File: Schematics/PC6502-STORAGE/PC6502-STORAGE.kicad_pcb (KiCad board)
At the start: 4 copper layers, 100 x 100 mm, 82 parts, among them J1 BUS, J2 Conn_02x26_Top_Bottom, J3 CLK_SLOW, J5 USB_C_Receptacle_USB2.0_16P, J6 ST4500 PROG, J7 Conn_02x05_Odd_Even, J8 TF-15X15, J99 Conn_02x05_Odd_Even, Q1 STL9P3LLH6, U1 ATF1502AS, U2 STUSB4500QTR, U3 ATF1502AS, U4 TXB0108PW, U5 AMS1117-3.3

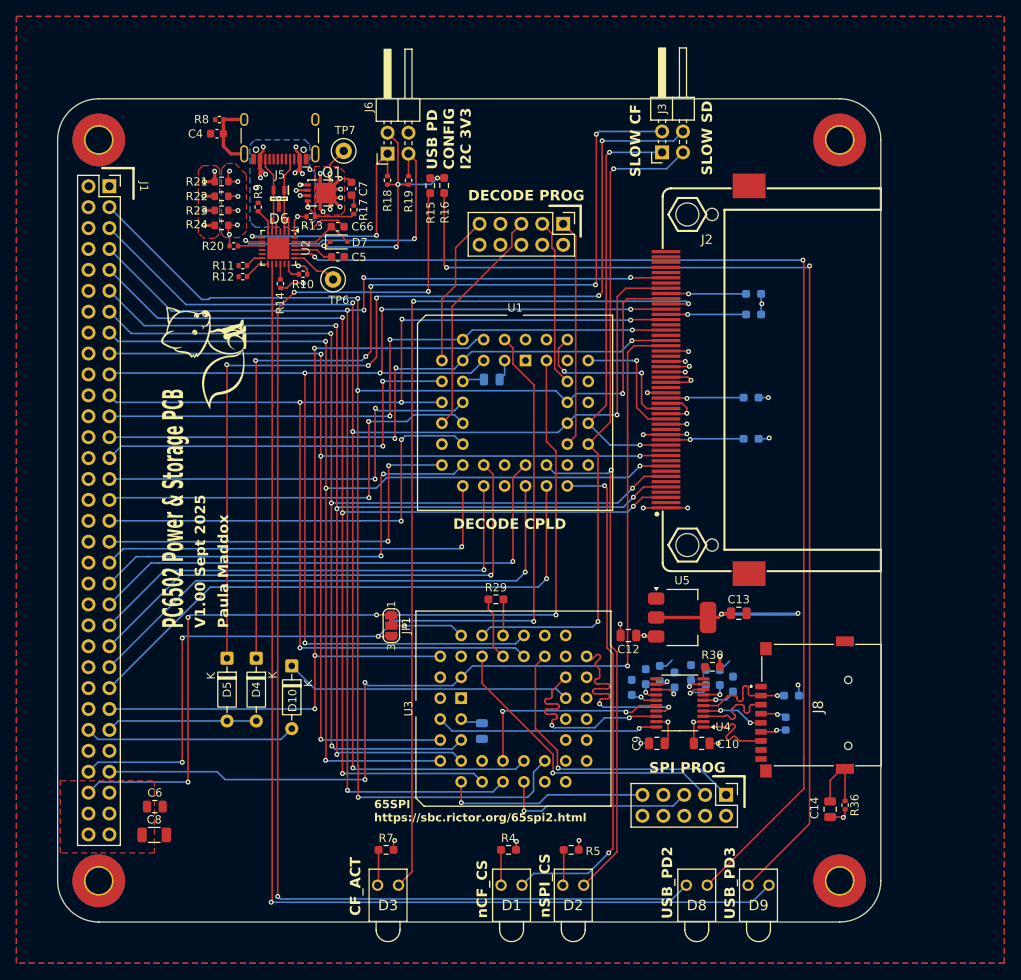
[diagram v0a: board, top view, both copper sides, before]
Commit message: Tidy up and simplify
Created schematic for FM & Speech sound board
Made Storage board just for Compact Flash (CF) storage
Routed Storage PCB
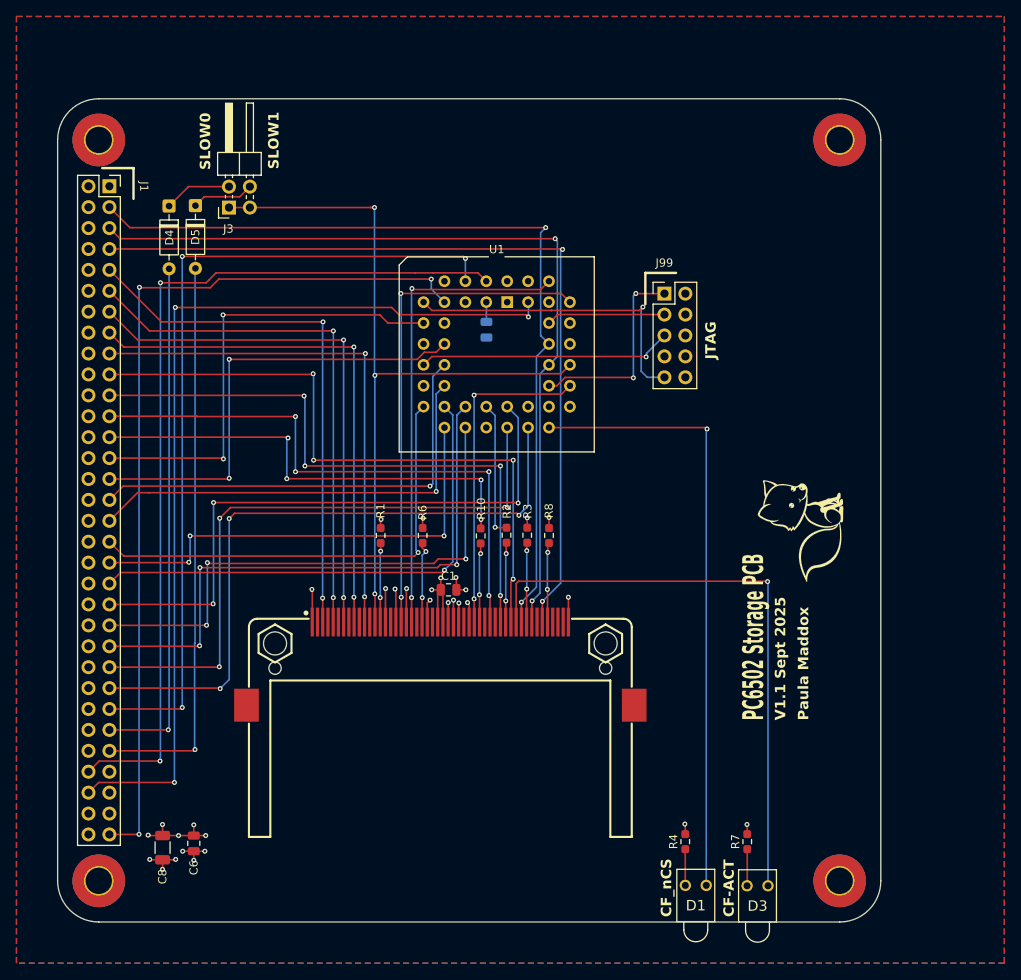
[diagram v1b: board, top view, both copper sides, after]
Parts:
- removed C10, C9: 100nF, Capacitor_SMD:C_0805_2012Metric
- removed C11, C7: 0.1uF, Capacitor_SMD:C_0603_1608Metric
- removed C12, C13: 10uF, Capacitor_SMD:C_0805_2012Metric
- removed C14: 100nF 100V, Capacitor_SMD:C_0805_2012Metric
- removed C4: 100nF 100V, Capacitor_SMD:C_0603_1608Metric
- removed C5, C66: 1uF, Capacitor_SMD:C_0603_1608Metric
- removed D10: 1N4148, Diode_THT:D_DO-35_SOD27_P7.62mm_Horizontal
- removed D2, D8, D9: LED, LTL-4221NHBP:LTL4221NHBP
- removed D6: ESDA25W, ESDA25W:SOT65P210X110-3N
- removed D7: BAT60A, Diode_SMD:D_SOD-323
- removed J5: USB_C_Receptacle_USB2.0_16P, Connector_USB:USB_C_Receptacle_HCTL_HC-TYPE-C-16P-01A
- removed J6: ST4500 PROG, Connector_PinHeader_2.54mm:PinHeader_2x02_P2.54mm_Horizontal
- removed J7: Conn_02x05_Odd_Even, Connector_PinHeader_2.54mm:PinHeader_2x05_P2.54mm_Vertical
- removed J8: TF-15X15, TF-15X15:TF15X15
- removed JP1: Jumper_3_Bridged12, Jumper:SolderJumper-3_P1.3mm_Bridged12_RoundedPad1.0x1.5mm_NumberLabels
- removed Q1: STL9P3LLH6, STL9P3LLH6:STL20N6F7
- removed R11, R12, R18, R19: 5K1, Resistor_SMD:R_0402_1005Metric
- removed R13, R9: 100K, Resistor_SMD:R_0402_1005Metric
- removed R14: 22K, Resistor_SMD:R_0402_1005Metric
- removed R15, R16, R5: 470R, Resistor_SMD:R_0603_1608Metric_Pad0.98x0.95mm_HandSolder
- removed R17: 100R, Resistor_SMD:R_0402_1005Metric
- removed R20: 1K, Resistor_SMD:R_0402_1005Metric
- removed R21, R22, R23, R24: 0R, Resistor_SMD:R_0603_1608Metric
- removed R25, R26, R27, R28, R29, R30, R31, R32, R33, R34, R35: 10K, Resistor_SMD:R_0603_1608Metric_Pad0.98x0.95mm_HandSolder
- removed R36: 330R, Resistor_SMD:R_0402_1005Metric
- removed TP6, TP7: TestPoint, TestPoint:TestPoint_Loop_D1.80mm_Drill1.0mm_Beaded
- removed U2: STUSB4500QTR, Package_DFN_QFN:QFN-24-1EP_4x4mm_P0.5mm_EP2.7x2.7mm
- removed U3: ATF1502AS, Package_LCC:PLCC-44_THT-Socket
- removed U4: TXB0108PW, Package_SO:TSSOP-20_4.4x6.5mm_P0.65mm
- removed U5: AMS1117-3.3, Package_TO_SOT_SMD:SOT-223-3_TabPin2
- C1, R1, R2, R3, R6: moved to F.Cu
- R10: value 1K -> 0R; footprint Resistor_SMD:R_0402_1005Metric -> Resistor_SMD:R_0603_1608Metric_Pad0.98x0.95mm_HandSolder
- R8: value 330R -> 1K; footprint Resistor_SMD:R_0402_1005Metric -> Resistor_SMD:R_0603_1608Metric_Pad0.98x0.95mm_HandSolder
- moved FOX1 75.5 mm to (187.3, 96.8)
- moved R8 64.5 mm to (156.8, 98.0), turned to 90 degrees
- moved D4 55.9 mm to (110.6, 58.0)
- moved D5 55.1 mm to (113.8, 58.0)
- moved J3 53.0 mm to (117.9, 58.2)
- moved C2 48.8 mm to (149.2, 73.0)
- moved J2 47.4 mm to (143.6, 113.6), turned to 0 degrees
- moved R1 46.5 mm to (136.3, 98.0), turned to 90 degrees
- moved D3 44.9 mm to (180.8, 140.6)
- moved R7 43.9 mm to (180.8, 135.2), turned to 90 degrees
- moved R6 43.3 mm to (141.4, 98.0), turned to 90 degrees
- moved R2 40.2 mm to (151.6, 98.0), turned to 90 degrees
- moved R3 40.2 mm to (154.1, 98.0), turned to 90 degrees
- moved R10 38.4 mm to (148.4, 98.1), turned to 90 degrees
- moved C1 26.1 mm to (144.6, 104.7), turned to 0 degrees
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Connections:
- net CLK renamed SYSCLK
- D4 pad 2: nSLOW -> nSLOW0
- D5 pad 2: nSLOW -> nSLOW1
- J1 pad 12: GND -> +5V
- J1 pad 16: GND -> +5V
- J1 pad 20: GND -> +5V
- J1 pad 24: GND -> +5V
- J1 pad 28: GND -> +5V
- J1 pad 32: GND -> +5V
- J1 pad 36: GND -> +5V
- J1 pad 4: GND -> +5V
- J1 pad 40: GND -> +5V
- J1 pad 44: GND -> +5V
- J1 pad 48: GND -> +5V
- J1 pad 53: nSLOW -> nSLOW0
- J1 pad 55: nBUSRQ -> nSLOW1
- J1 pad 57: nRES -> RDY
- J1 pad 59: +5V -> nVP
- J1 pad 61: +5V -> nBUSRQ
- J1 pad 62: +5V -> unconnected-(J1-Pin_62-Pad62)
- J1 pad 63: +5V -> nRES
- J1 pad 64: +5V -> GND
- J1 pad 8: GND -> +5V
- J2 pad 17: /A3 -> Net-(J2-Pin_17)
- J2 pad 41: nRES -> CFnRES
- J2 pad 48: unconnected-(J2-Pin_48-Pad48) -> Net-(J2-Pin_48)
- J2 pad 7: nCF_CS -> nCF_CS0
- J3 pad 1: nCF_CS -> nCF_CS0
- J3 pad 3: nSPI_CS -> nCF_CS0
- R10 pad 1: Net-(U2-VBUS_VS_DISCH) -> Net-(J2-Pin_17)
- R10 pad 2: /USB Power/VIN -> /A3
- R8 pad 1: GND -> Net-(J2-Pin_48)
- R8 pad 2: Net-(J5-SHIELD) -> +5V
- U1 pad 11: /A1 -> unconnected-(U1-I/O/PD1-Pad11)
- U1 pad 27: nSPI_LED -> unconnected-(U1-I/O-Pad27)
- U1 pad 31: nSPI_CS -> CFnRES
- U1 pad 33: nCF_CS -> nCF_CS0
- U1 pad 5: /A0 -> unconnected-(U1-I/O-Pad5)
- U1 pad 6: /A2 -> unconnected-(U1-I/O-Pad6)
- U1 pad 8: /A3 -> nRES
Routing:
- net Net-(D8-A): track 153.0 -> 0.00 mm, vias 3 -> 0
- net Net-(D8-K): track 142.9 -> 0.00 mm, vias 2 -> 0
- net Net-(D9-K): track 138.9 -> 0.00 mm, vias 1 -> 0
- net Net-(D9-A): track 131.7 -> 0.00 mm, vias 2 -> 0
- net Net-(D5-K): track 117.9 -> 7.57 mm, vias 5 -> 0
- net Net-(D4-K): track 112.4 -> 8.25 mm, vias 5 -> 0
- net nCF_CS0: track 0.00 -> 92.3 mm, vias 0 -> 3
- net nSPI_CS: track 80.8 -> 0.00 mm, vias 2 -> 0
- net /D3: track 143.6 -> 65.1 mm, vias 4 -> 2
- net /D4: track 138.1 -> 64.6 mm, vias 4 -> 2
- net /D5: track 136.4 -> 64.1 mm, vias 4 -> 2
- net /D6: track 134.0 -> 63.8 mm, vias 4 -> 2
- net /A0: track 148.4 -> 79.3 mm, vias 5 -> 4
- net nSLOW1: track 0.00 -> 69.0 mm, vias 0 -> 1
- net /D0: track 171.1 -> 104.0 mm, vias 4 -> 2
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- removed copper zone on F.Cu, net +5V
- removed copper zone on B.Cu, net /USB Power/VIN
- removed copper zone on F.Cu, net /USB Power/VUSB_SW
- removed copper zone on In1.Cu, net /USB Power/VUSB_SW
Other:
- board text added: "CF-ACT"
- board text added: "CF_nCS"
- board text added: "JTAG"
- board text added: "PC6502 Storage PCB"
- board text added: "SLOW0"
- board text added: "SLOW1"
- board text added: "V1.1 Sept 2025"
- board text removed: "65SPI https://sbc.rictor.org/65spi2.html"
- board text removed: "CF_ACT"
- board text removed: "DECODE CPLD"
- board text removed: "DECODE PROG"
- board text removed: "PC6502 Power & Storage PCB"
- board text removed: "SLOW CF"
- board text removed: "SLOW SD"
- board text removed: "SPI PROG"
- board text removed: "USB PD CONFIG I2C 3V3"
- board text removed: "USB_PD2"
- board text removed: "USB_PD3"
- board text removed: "V1.00 Sept 2025"
- board text removed: "nCF_CS"
- board text removed: "nSPI_CS"
